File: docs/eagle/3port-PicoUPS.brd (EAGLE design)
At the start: 57.2 x 69.8 mm, 59 parts, among them IC1 MAX471CPA, IC2 MAX471CPA, IC3 MAX471CPA, IC4 REG1117, K1 APF30212C, K2 APF30212C, K3 APF30212C, Q1 MMBT2222A, Q2 MMBT2222A, Q3 MMBT2222A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

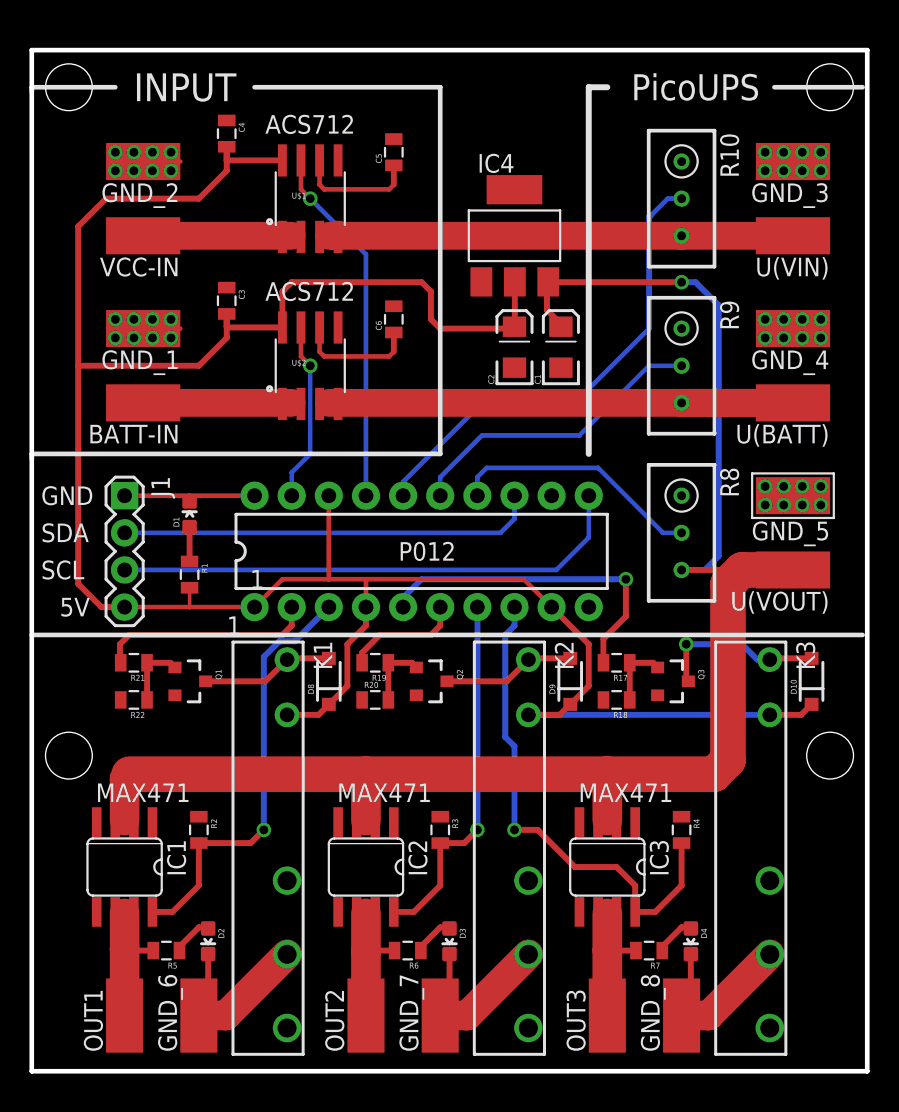
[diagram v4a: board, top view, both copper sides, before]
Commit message: Swap out AMS1117 for LM7805, as the former has max voltage of 15V, while we're running at 18V - LM7805 is rated to 20V
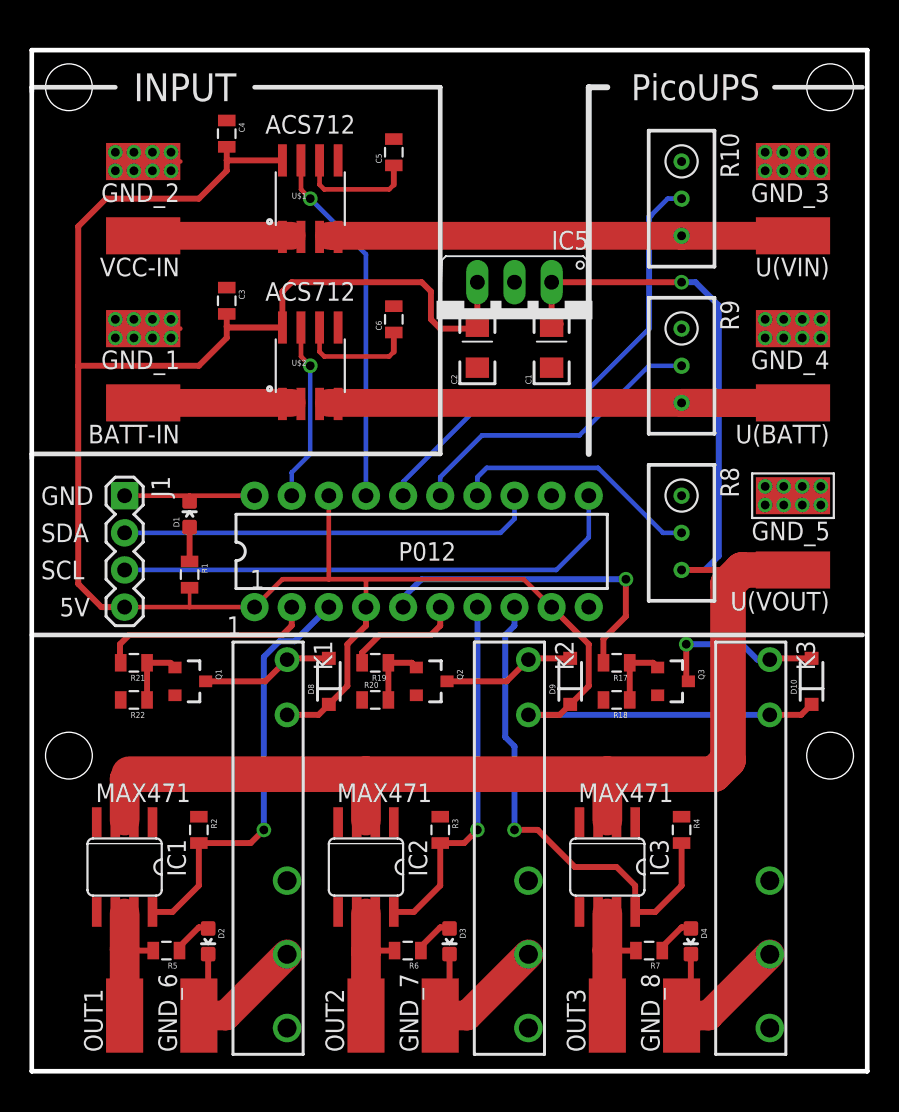
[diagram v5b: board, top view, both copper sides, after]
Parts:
- removed IC4: REG1117, burr-brown:SOT223
- added IC5: 7805TV, linear:TO220V
- moved C2 2.54 mm to (26.7, 58.4)
- moved C1 0.63 mm to (31.8, 58.4)
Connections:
- net 12V: now also IC5.1; no longer IC4.3
- net 5V: now also IC5.3; no longer IC4.2
- net GND: now also IC5.2; no longer IC4.1
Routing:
- net 5V: track 169.0 -> 165.3 mm
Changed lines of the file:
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@@
 <attribute name="PROD_ID" value="CONN-09696" x="2.54" y="48.26" size="1.778" layer="27" rot="R270" display="off"/>
 </element>
-<element name="IC4" library="burr-brown" package="SOT223" value="REG1117" x="29.21" y="66.04">
-<attribute name="MF" value="" x="29.21" y="66.04" size="1.778" layer="27" display="off"/>
-<attribute name="MPN" value="REG1117" x="29.21" y="66.04" size="1.778" layer="27" display="off"/>
-<attribute name="OC_FARNELL" value="1097566" x="29.21" y="66.04" size="1.778" layer="27" display="off"/>
-<attribute name="OC_NEWARK" value="14P6981" x="29.21" y="66.04" size="1.778" layer="27" display="off"/>
-</element>
-<element name="C1" library="SparkFun-Capacitors" package="EIA3216" value="10uF" x="32.385" y="58.42" rot="R90">
-<attribute name="PROD_ID" value="CAP-00811" x="32.385" y="58.42" size="1.778" layer="27" rot="R90" display="off"/>
-</element>
-<element name="C2" library="SparkFun-Capacitors" package="EIA3216" value="10uF" x="29.21" y="58.42" rot="R90">
-<attribute name="PROD_ID" value="CAP-00811" x="29.21" y="58.42" size="1.778" layer="27" rot="R90" display="off"/>
+<element name="C1" library="SparkFun-Capacitors" package="EIA3216" value="10uF" x="31.75" y="58.42" rot="R90">
+<attribute name="PROD_ID" value="CAP-00811" x="31.75" y="58.42" size="1.778" layer="27" rot="R90" display="off"/>
+</element>
+<element name="C2" library="SparkFun-Capacitors" package="EIA3216" value="10uF" x="26.67" y="58.42" rot="R90">
+<attribute name="PROD_ID" value="CAP-00811" x="26.67" y="58.42" size="1.778" layer="27" rot="R90" display="off"/>
 </element>
 <element name="K1" library="relay" package="APF30212C" value="APF30212C" x="13.6525" y="24.4475" rot="R270">
@@
 <element name="C4" library="SparkFun-Capacitors" package="0805" value="100n" x="9.525" y="73.025" rot="R270"/>
 <element name="C6" library="SparkFun-Capacitors" package="0805" value="1n" x="20.955" y="60.325" rot="R90"/>
+<element name="IC5" library="linear" package="TO220V" value="7805TV" x="29.21" y="60.325" rot="R180"/>
 </elements>
 <signals>
@@
 <contactref element="U(VOUT)" pad="1"/>
 <contactref element="C1" pad="A"/>
-<contactref element="IC4" pad="3"/>
-<wire x1="40.64" y1="43.18" x2="42.2275" y2="43.18" width="0.4064" layer="16"/>
-<wire x1="42.2275" y1="43.18" x2="43.18" y2="44.1325" width="0.4064" layer="16"/>
-<wire x1="43.18" y1="44.1325" x2="43.18" y2="61.2775" width="0.4064" layer="16"/>
-<wire x1="43.18" y1="61.2775" x2="41.5925" y2="62.865" width="0.4064" layer="16"/>
-<wire x1="41.5925" y1="62.865" x2="40.64" y2="62.865" width="0.4064" layer="16"/>
-<via x="40.64" y="62.865" extent="1-16" drill="0.6" shape="square"/>
-<wire x1="40.64" y1="62.865" x2="32.0675" y2="62.865" width="0.4064" layer="1"/>
-<wire x1="31.5214" y1="62.8904" x2="32.0421" y2="62.8904" width="0.4064" layer="1"/>
-<wire x1="32.0421" y1="62.8904" x2="32.0675" y2="62.865" width="0.4064" layer="1"/>
-<wire x1="32.385" y1="59.82" x2="32.385" y2="60.0075" width="0.4064" layer="1"/>
-<wire x1="32.385" y1="60.0075" x2="31.4325" y2="60.96" width="0.4064" layer="1"/>
-<wire x1="31.4325" y1="60.96" x2="31.4325" y2="62.8015" width="0.4064" layer="1"/>
-<wire x1="31.4325" y1="62.8015" x2="31.5214" y2="62.8904" width="0.4064" layer="1"/>
+<wire x1="32.385" y1="60.0075" x2="31.75" y2="59.82" width="0.4064" layer="1"/>
 <wire x1="48.26" y1="43.18" x2="44.7675" y2="43.18" width="2.4384" layer="1"/>
 <wire x1="44.7675" y1="43.18" x2="43.815" y2="42.2275" width="2.4384" layer="1"/>
@@
 <wire x1="3.175" y1="25.9334" x2="2.6416" y2="25.9334" width="0.4064" layer="1"/>
 <wire x1="2.6416" y1="25.9334" x2="2.54" y2="26.035" width="0.4064" layer="1"/>
-<wire x1="35.509334375" y1="29.21" x2="19.05" y2="29.21" width="2.4384" layer="1"/>
+<wire x1="35.56" y1="29.21" x2="19.05" y2="29.21" width="2.4384" layer="1"/>
 <wire x1="19.05" y1="29.21" x2="2.8575" y2="29.21" width="2.4384" layer="1"/>
-<wire x1="35.509334375" y1="29.21" x2="42.8625" y2="29.21" width="2.4384" layer="1"/>
-<wire x1="35.56" y1="29.21" x2="35.509334375" y2="29.21" width="2.4384" layer="1"/>
+<wire x1="35.56" y1="29.21" x2="42.8625" y2="29.21" width="2.4384" layer="1"/>
 <wire x1="19.685" y1="25.9334" x2="19.685" y2="28.575" width="0.4064" layer="1"/>
 <wire x1="19.685" y1="28.575" x2="19.05" y2="29.21" width="0.4064" layer="1"/>
+<wire x1="31.5214" y1="60.0486" x2="31.75" y2="59.82" width="0.4064" layer="1"/>
+<contactref element="IC5" pad="1"/>
+<wire x1="31.75" y1="59.82" x2="31.75" y2="62.865" width="0.4064" layer="1"/>
+<wire x1="31.75" y1="62.865" x2="40.64" y2="62.865" width="0.4064" layer="1"/>
+<via x="40.64" y="62.865" extent="1-16" drill="0.6" shape="square"/>
+<wire x1="40.64" y1="62.865" x2="41.5925" y2="62.865" width="0.4064" layer="16"/>
+<wire x1="41.5925" y1="62.865" x2="43.18" y2="61.2775" width="0.4064" layer="16"/>
+<wire x1="43.18" y1="61.2775" x2="43.18" y2="44.1325" width="0.4064" layer="16"/>
+<wire x1="43.18" y1="44.1325" x2="42.2275" y2="43.18" width="0.4064" layer="16"/>
+<wire x1="42.2275" y1="43.18" x2="40.64" y2="43.18" width="0.4064" layer="16"/>
 </signal>
 <signal name="GND">
@@
 <vertex x="-3.81" y="8.89"/>
 </polygon>
-<contactref element="IC4" pad="1"/>
 <contactref element="C1" pad="C"/>
 <contactref element="C2" pad="C"/>
@@
 <contactref element="C6" pad="2"/>
 <contactref element="C4" pad="1"/>
+<contactref element="IC5" pad="2"/>
 </signal>
 <signal name="V-UPS">
@@
 <wire x1="6.97755625" y1="40.64" x2="11.43" y2="40.64" width="0.3175" layer="1"/>
 <wire x1="6.97755625" y1="40.64" x2="2.54" y2="40.64" width="0.3175" layer="1"/>
-<contactref element="IC4" pad="2"/>
 <contactref element="C2" pad="A"/>
-<wire x1="29.2354" y1="62.8904" x2="29.2354" y2="59.8454" width="0.4064" layer="1"/>
-<wire x1="29.2354" y1="59.8454" x2="29.21" y2="59.82" width="0.4064" layer="1"/>
 <wire x1="13.335" y1="62.23" x2="13.335" y2="59.7662" width="0.4064" layer="1"/>
 <wire x1="13.335" y1="62.23" x2="13.97" y2="62.865" width="0.4064" layer="1"/>
@@
 <wire x1="23.495" y1="62.23" x2="23.495" y2="60.325" width="0.4064" layer="1"/>
 <wire x1="23.495" y1="60.325" x2="24.13" y2="59.69" width="0.4064" layer="1"/>
-<wire x1="24.13" y1="59.69" x2="29.08" y2="59.69" width="0.4064" layer="1"/>
-<wire x1="29.08" y1="59.69" x2="29.21" y2="59.82" width="0.4064" layer="1"/>
 <contactref element="K2" pad="2"/>
 <contactref element="K1" pad="2"/>
@@
 <wire x1="7.62" y1="57.15" x2="9.525" y2="59.055" width="0.4064" layer="1"/>
 <wire x1="9.525" y1="59.834034375" x2="9.525" y2="59.055" width="0.4064" layer="1"/>
-<wire x1="9.525" y1="59.834034375" x2="9.525" y2="60.39485" width="0.4064" layer="1"/>
+<wire x1="9.525" y1="59.834034375" x2="9.525" y2="60.695" width="0.4064" layer="1"/>
 <wire x1="13.335" y1="59.7662" x2="9.592834375" y2="59.7662" width="0.4064" layer="1"/>
 <wire x1="9.592834375" y1="59.7662" x2="9.525" y2="59.834034375" width="0.4064" layer="1"/>
@@
 <wire x1="7.62" y1="68.58" x2="9.525" y2="70.485" width="0.4064" layer="1"/>
 <wire x1="9.525" y1="71.206" x2="9.525" y2="70.485" width="0.4064" layer="1"/>
-<wire x1="9.525" y1="71.206" x2="9.525" y2="71.82485" width="0.4064" layer="1"/>
+<wire x1="9.525" y1="71.206" x2="9.525" y2="72.125" width="0.4064" layer="1"/>
 <wire x1="13.335" y1="71.1962" x2="9.5348" y2="71.1962" width="0.4064" layer="1"/>
 <wire x1="9.5348" y1="71.1962" x2="9.525" y2="71.206" width="0.4064" layer="1"/>
-<wire x1="9.525" y1="60.695" x2="9.525" y2="59.834034375" width="0.4064" layer="1"/>
-<wire x1="9.525" y1="72.125" x2="9.525" y2="71.206" width="0.4064" layer="1"/>
+<contactref element="IC5" pad="3"/>
+<wire x1="24.13" y1="59.69" x2="26.54" y2="59.69" width="0.4064" layer="1"/>
+<wire x1="26.54" y1="59.69" x2="26.67" y2="59.82" width="0.4064" layer="1"/>
+<wire x1="26.67" y1="59.82" x2="26.67" y2="62.865" width="0.4064" layer="1"/>
 </signal>
 <signal name="VCC-UPS">

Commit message: Cosmetic changes - flip the direction of R20 (to be the same as R18/R22); also straighten the VBATT and VIN traces on the righthand side J4 and J6; also move the labels 'MAX471' up a bit so they are not in the solder mask
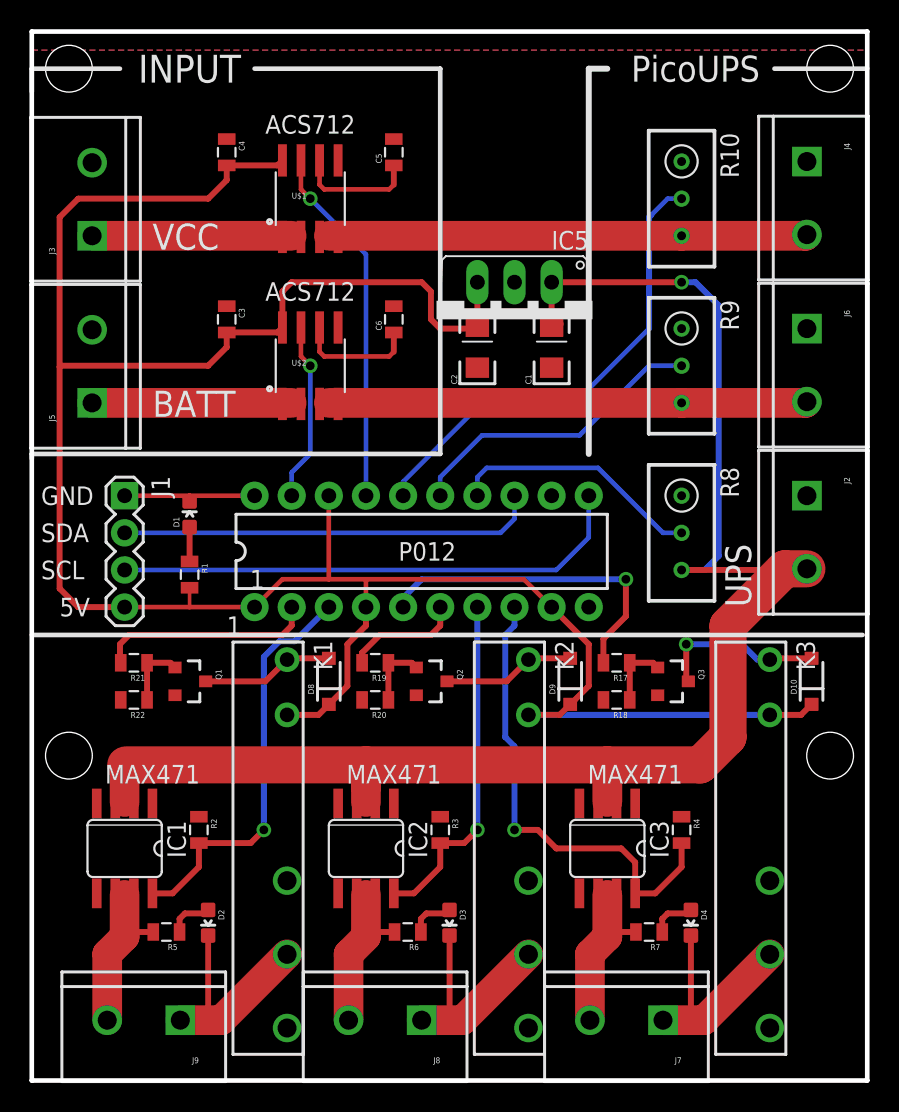
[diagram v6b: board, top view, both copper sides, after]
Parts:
- removed BATT-IN, OUT1, OUT2, OUT3, U(BATT), U(VIN), U(VOUT): 12V, wirepad:SMD2,54-5,08
- removed GND_1, GND_3, GND_4, GND_6, GND_7, GND_8: WIREPADSMD2,54-5,08, wirepad:SMD2,54-5,08
- removed GND_2: -, wirepad:SMD2,54-5,08
- removed GND_5: WIREPADSMD5-2,5, wirepad:5-2,5
- removed VCC-IN: +, wirepad:SMD2,54-5,08
- added J2, J3, J4, J5, J6, J7, J8, J9: (no value), SparkFun-Connectors:SCREWTERMINAL-5MM-2
- moved C4 1.27 mm to (9.53, 71.8)
- moved D2 1.27 mm to (8.26, 19.1)
- moved D3 1.27 mm to (24.8, 19.1)
- moved D4 1.27 mm to (41.3, 19.1)
- moved IC1 1.27 mm to (2.54, 24.1)
- moved IC2 1.27 mm to (19.1, 24.1)
- moved IC3 1.27 mm to (35.6, 24.1)
- moved R5 1.27 mm to (5.40, 18.4)
- moved R6 1.27 mm to (21.9, 18.4)
- moved R7 1.27 mm to (38.4, 18.4)
- moved C3 1.27 mm to (9.53, 60.3)
- turned R20 to 180 degrees
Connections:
- net 12V: now also J2.2; no longer U(VOUT).1
- net BATT: now also J5.1; no longer BATT-IN.1
- net BATT-UPS: now also J6.2; no longer U(BATT).1
- net GND: now also J2.1, J3.2, J4.1, J5.2, J6.1, R20.2; no longer GND_1.1, GND_2.1, GND_3.1, GND_4.1, GND_5.1, R20.1
- net GND_6: now also J9.1; no longer GND_6.1
- net GND_7: now also J8.1; no longer GND_7.1
- net GND_8: now also J7.1; no longer GND_8.1
- net N$13: now also R20.1; no longer R20.2
- net OUT1: now also J9.2; no longer OUT1.1
- net OUT2: now also J8.2; no longer OUT2.1
- net OUT3: now also J7.2; no longer OUT3.1
- net VCC: now also J3.1; no longer VCC-IN.1
- net VCC-UPS: now also J4.2; no longer U(VIN).1
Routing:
- net GND: track 17.0 -> 9.28 mm, vias 40 -> 0
- net BATT-UPS: track 40.7 -> 34.1 mm
- net 12V: track 115.8 -> 120.3 mm
- net BATT: track 11.5 -> 15.0 mm
- net VCC: track 11.5 -> 15.0 mm
- net GND_8: track 12.2 -> 15.3 mm
- net GND_6: track 12.2 -> 15.3 mm
- net GND_7: track 12.2 -> 15.3 mm
- net 5V: track 165.3 -> 168.1 mm
- net OUT3: track 10.3 -> 12.5 mm
- net OUT2: track 10.4 -> 12.6 mm
- net OUT1: track 10.5 -> 12.5 mm
- net VCC-UPS: track 32.8 -> 34.1 mm
- net I2: track 25.0 -> 23.7 mm
- net I1: track 29.3 -> 28.1 mm
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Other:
- board size 57.2 x 69.8 mm -> 57.2 x 71.8 mm
- board text added: "BATT"
- board text added: "UPS"
- board text added: "VCC"
- board text added: "pim@ipng.nl Version 1.3 github.com/pimvanpelt"
- board text removed: "pim@ipng.nl Version 1.2 github.com/pimvanpelt"

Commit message: Replace potis with fixed voltage dividers at 3k9 : 1k each which will give me 24.5V of range. 15V input will now read 3.061V on the ADC inputs.
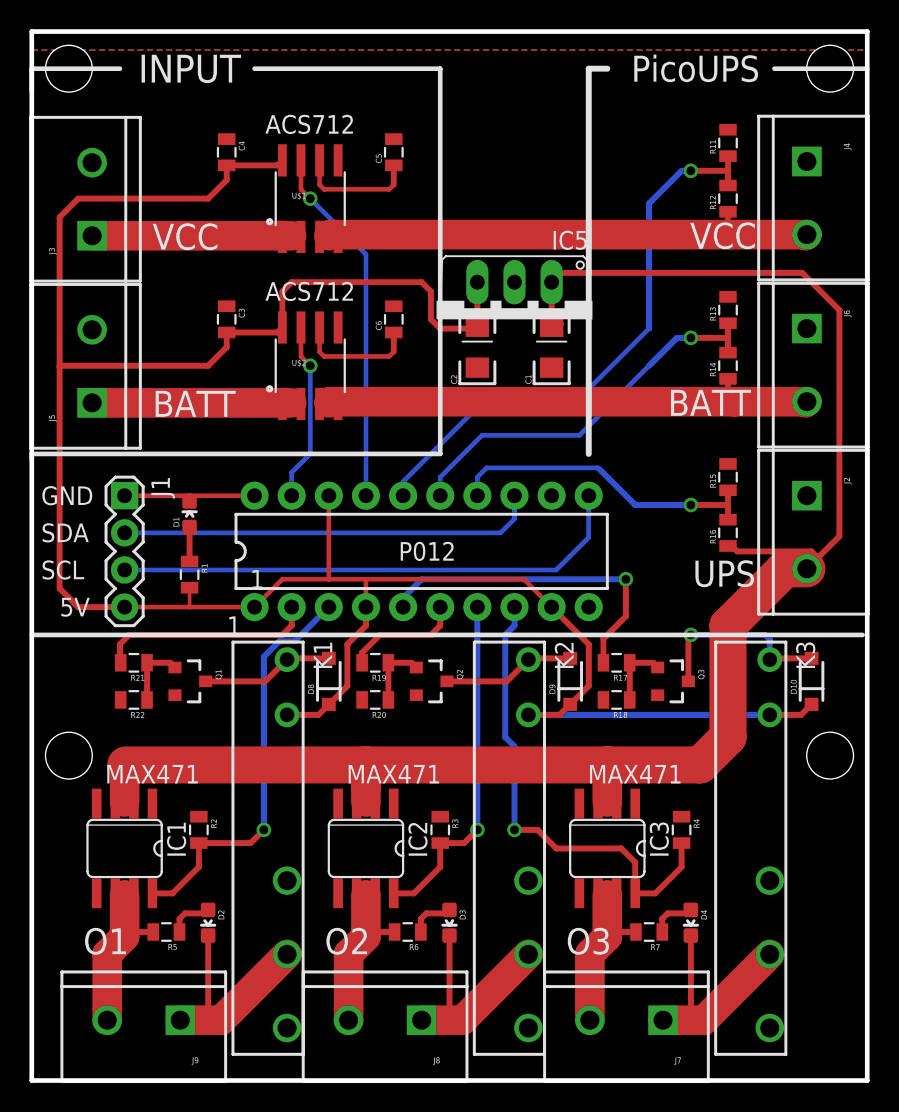
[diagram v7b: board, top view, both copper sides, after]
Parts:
- removed R10, R8, R9: 10k, rcl:RTRIM3296W
- added R11, R13, R15: 3k9, SparkFun-Passives:0805
- added R12, R14, R16: 1k, SparkFun-Passives:0805
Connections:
- net 12V: now also R16.1; no longer R8.3
- net BATT-UPS: now also R14.1; no longer R9.3
- net GND: now also R11.2, R13.2, R15.2; no longer R10.1, R8.1, R9.1
- net V-BATT: now also R13.1, R14.2; no longer R9.2
- net V-UPS: now also R15.1, R16.2; no longer R8.2
- net V-VCC: now also R11.1, R12.2; no longer R10.2
- net VCC-UPS: now also R12.1; no longer R10.3
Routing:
- net V-VCC: track 32.5 -> 39.0 mm, vias 0 -> 1
- net V-BATT: track 20.9 -> 26.9 mm, vias 0 -> 1
- net 12V: track 120.3 -> 125.8 mm, vias 1 -> 0
- net V-UPS: track 17.3 -> 21.7 mm, vias 0 -> 1
- net BATT-UPS: track 34.1 -> 35.9 mm
- net VCC-UPS: track 34.1 -> 35.8 mm
- net N$10: track 11.6 -> 13.2 mm
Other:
- board text added: "O1"
- board text added: "O2"
- board text added: "O3"
- board text added: "pim@ipng.nl Version 1.4 github.com/pimvanpelt"
- board text removed: "pim@ipng.nl Version 1.3 github.com/pimvanpelt"
